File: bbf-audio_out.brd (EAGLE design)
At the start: 21.6 x 54.6 mm, 13 parts, among them IC1 TL072P, J5 MONOSWSLIM

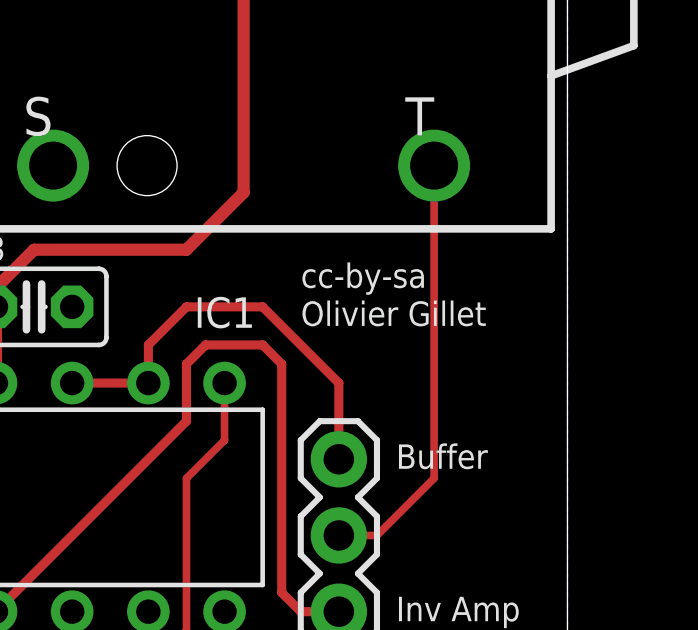
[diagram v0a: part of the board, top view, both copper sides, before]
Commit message: update names on boards and schematics
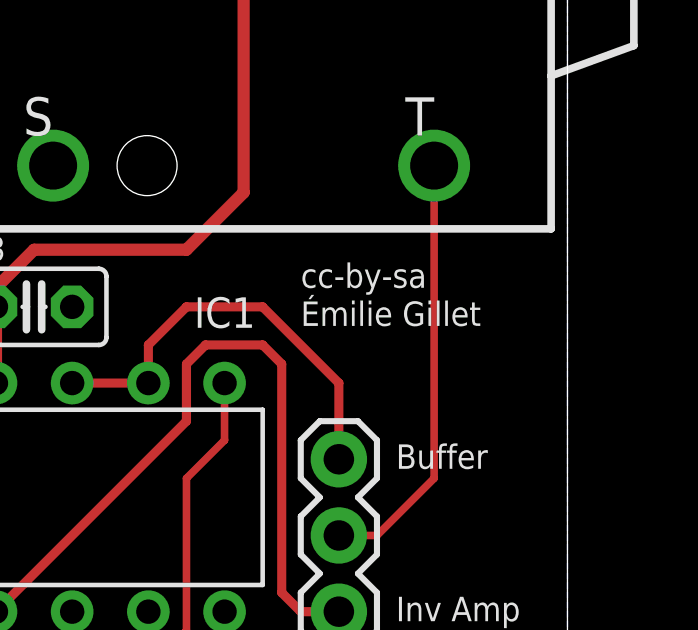
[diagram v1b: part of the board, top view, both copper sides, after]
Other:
- board text added: "Émilie Gillet"
- board text removed: "Olivier Gillet"
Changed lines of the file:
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@@
 <text x="25.4" y="33.9725" size="0.8128" layer="21" ratio="15">&gt;Out</text>
 <text x="22.225" y="42.545" size="0.8128" layer="25" ratio="15">cc-by-sa</text>
-<text x="22.225" y="41.275" size="0.8128" layer="25" ratio="15">Olivier Gillet</text>
+<text x="22.225" y="41.275" size="0.8128" layer="25" ratio="15">Émilie Gillet</text>
 </plain>
 <attributes>
